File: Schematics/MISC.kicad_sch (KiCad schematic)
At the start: 7 parts, among them J6 I2C Header, J7 PWR, J8 I2S Header

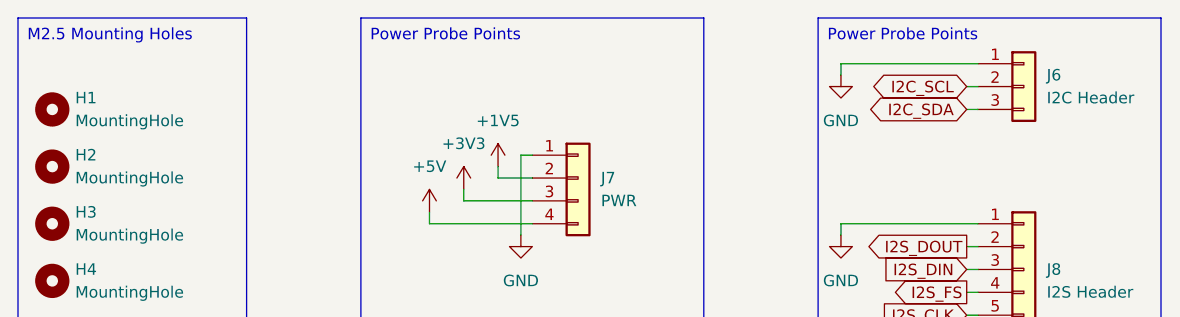
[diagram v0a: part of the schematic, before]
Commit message: Updated to KiCAD v9
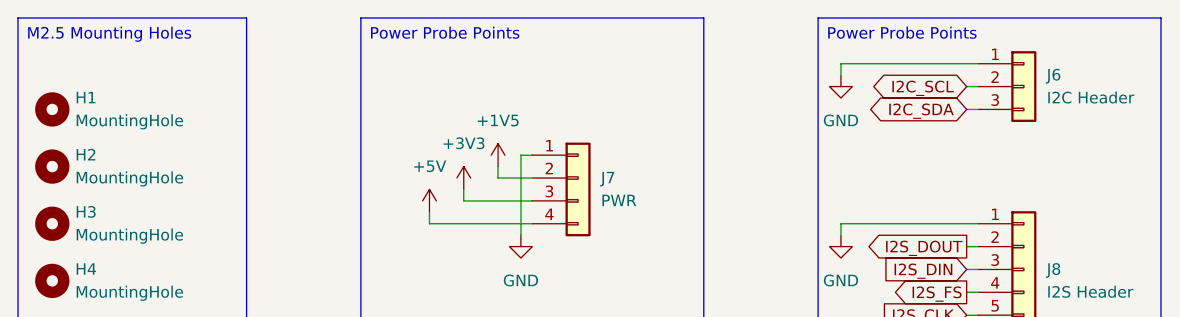
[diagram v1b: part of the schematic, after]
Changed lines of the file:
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@@
 (kicad_sch
-	(version 20231120)
+	(version 20250114)
 	(generator "eeschema")
-	(generator_version "8.0")
+	(generator_version "9.0")
 	(paper "A4")
-	(wire
-		(pts
-			(xy 116.84 31.75) (xy 116.84 30.48)
-		)
-		(stroke
-			(width 0)
-			(type default)
-		)
-	)
-	(wire
-		(pts
-			(xy 116.84 30.48) (xy 132.08 30.48)
-		)
-		(stroke
-			(width 0)
-			(type default)
-		)
-	)
-	(wire
-		(pts
-			(xy 74.93 45.72) (xy 74.93 44.45)
-		)
-		(stroke
-			(width 0)
-			(type default)
-		)
-	)
-	(wire
-		(pts
-			(xy 130.81 60.96) (xy 132.08 60.96)
-		)
-		(stroke
-			(width 0)
-			(type default)
-		)
-	)
-	(wire
-		(pts
-			(xy 130.81 58.42) (xy 132.08 58.42)
-		)
-		(stroke
-			(width 0)
-			(type default)
-		)
-	)
-	(wire
-		(pts
-			(xy 132.08 48.26) (xy 116.84 48.26)
-		)
-		(stroke
-			(width 0)
-			(type default)
-		)
-	)
-	(wire
-		(pts
-			(xy 130.81 35.56) (xy 132.08 35.56)
-		)
-		(stroke
-			(width 0)
-			(type default)
-		)
-	)
-	(wire
-		(pts
-			(xy 130.81 50.8) (xy 132.08 50.8)
-		)
-		(stroke
-			(width 0)
-			(type default)
-		)
-	)
-	(wire
-		(pts
-			(xy 130.81 33.02) (xy 132.08 33.02)
-		)
-		(stroke
-			(width 0)
-			(type default)
-		)
-	)
-	(wire
-		(pts
-			(xy 130.81 53.34) (xy 132.08 53.34)
-		)
-		(stroke
-			(width 0)
-			(type default)
-		)
-	)
-	(wire
-		(pts
-			(xy 81.28 40.64) (xy 81.28 49.53)
-		)
-		(stroke
-			(width 0)
-			(type default)
-		)
-	)
-	(wire
-		(pts
-			(xy 81.28 40.64) (xy 82.55 40.64)
-		)
-		(stroke
-			(width 0)
-			(type default)
-		)
-	)
-	(wire
-		(pts
-			(xy 71.12 46.99) (xy 71.12 48.26)
-		)
-		(stroke
-			(width 0)
-			(type default)
-		)
-	)
-	(wire
-		(pts
-			(xy 130.81 55.88) (xy 132.08 55.88)
-		)
-		(stroke
-			(width 0)
-			(type default)
-		)
-	)
-	(wire
-		(pts
-			(xy 116.84 48.26) (xy 116.84 49.53)
-		)
-		(stroke
-			(width 0)
-			(type default)
-		)
-	)
-	(wire
-		(pts
-			(xy 71.12 48.26) (xy 82.55 48.26)
-		)
-		(stroke
-			(width 0)
-			(type default)
-		)
-	)
-	(wire
-		(pts
-			(xy 82.55 45.72) (xy 74.93 45.72)
-		)
-		(stroke
-			(width 0)
-			(type default)
-		)
-	)
-	(wire
-		(pts
-			(xy 78.74 43.18) (xy 82.55 43.18)
-		)
-		(stroke
-			(width 0)
-			(type default)
-		)
-	)
-	(wire
-		(pts
-			(xy 78.74 41.91) (xy 78.74 43.18)
-		)
-		(stroke
-			(width 0)
-			(type default)
-		)
-	)
 	(text_box "M2.5 Mounting Holes"
 		(exclude_from_sim no)
 		(at 25.4 25.4 0)
 		(size 25.4 38.1)
+		(margins 0.9525 0.9525 0.9525 0.9525)
 		(stroke
 			(width 0)
@@
 		(at 114.3 25.4 0)
 		(size 38.1 38.1)
+		(margins 0.9525 0.9525 0.9525 0.9525)
 		(stroke
 			(width 0)
@@
 		(at 63.5 25.4 0)
 		(size 38.1 38.1)
+		(margins 0.9525 0.9525 0.9525 0.9525)
 		(stroke
 			(width 0)
@@
 		)
 	)
+	(wire
+		(pts
+			(xy 116.84 31.75) (xy 116.84 30.48)
+		)
+		(stroke
+			(width 0)
+			(type default)
+		)
+	)
+	(wire
+		(pts
+			(xy 116.84 30.48) (xy 132.08 30.48)
+		)
+		(stroke
+			(width 0)
+			(type default)
+		)
+	)
+	(wire
+		(pts
+			(xy 74.93 45.72) (xy 74.93 44.45)
+		)
+		(stroke
+			(width 0)
+			(type default)
+		)
+	)
+	(wire
+		(pts
+			(xy 130.81 60.96) (xy 132.08 60.96)
+		)
+		(stroke
+			(width 0)
+			(type default)
+		)
+	)
+	(wire
+		(pts
+			(xy 130.81 58.42) (xy 132.08 58.42)
+		)
+		(stroke
+			(width 0)
+			(type default)
+		)
+	)
+	(wire
+		(pts
+			(xy 132.08 48.26) (xy 116.84 48.26)
+		)
+		(stroke
+			(width 0)
+			(type default)
+		)
+	)
+	(wire
+		(pts
+			(xy 130.81 35.56) (xy 132.08 35.56)
+		)
+		(stroke
+			(width 0)
+			(type default)
+		)
+	)
+	(wire
+		(pts
+			(xy 130.81 50.8) (xy 132.08 50.8)
+		)
+		(stroke
+			(width 0)
+			(type default)
+		)
+	)
+	(wire
+		(pts
+			(xy 130.81 33.02) (xy 132.08 33.02)
+		)
+		(stroke
+			(width 0)
+			(type default)
+		)
+	)
+	(wire
+		(pts
+			(xy 130.81 53.34) (xy 132.08 53.34)
+		)
+		(stroke
+			(width 0)
+			(type default)
+		)
+	)
+	(wire
+		(pts
+			(xy 81.28 40.64) (xy 81.28 49.53)
+		)
+		(stroke
+			(width 0)
+			(type default)
+		)
+	)
+	(wire
+		(pts
+			(xy 81.28 40.64) (xy 82.55 40.64)
+		)
+		(stroke
+			(width 0)
+			(type default)
+		)
+	)
+	(wire
+		(pts
+			(xy 71.12 46.99) (xy 71.12 48.26)
+		)
+		(stroke
+			(width 0)
+			(type default)
+		)
+	)
+	(wire
+		(pts
+			(xy 130.81 55.88) (xy 132.08 55.88)
+		)
+		(stroke
+			(width 0)
+			(type default)
+		)
+	)
+	(wire
+		(pts
+			(xy 116.84 48.26) (xy 116.84 49.53)
+		)
+		(stroke
+			(width 0)
+			(type default)
+		)
+	)
+	(wire
+		(pts
+			(xy 71.12 48.26) (xy 82.55 48.26)
+		)
+		(stroke
+			(width 0)
+			(type default)
+		)
+	)
+	(wire
+		(pts
+			(xy 82.55 45.72) (xy 74.93 45.72)
+		)
+		(stroke
+			(width 0)
+			(type default)
+		)
+	)
+	(wire
+		(pts
+			(xy 78.74 43.18) (xy 82.55 43.18)
+		)
+		(stroke
+			(width 0)
+			(type default)
+		)
+	)
+	(wire
+		(pts
+			(xy 78.74 41.91) (xy 78.74 43.18)
+		)
+		(stroke
+			(width 0)
+			(type default)
+		)
+	)

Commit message: File labelling
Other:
- note added: "Drawn by Harvey McBurney, Nicolas Viale"
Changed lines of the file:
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@@
 	(generator_version "9.0")
 	(paper "A4")
+	(text "Drawn by Harvey McBurney, Nicolas Viale"
+		(exclude_from_sim no)
+		(at 210.82 169.926 0)
+		(effects
+			(font
+				(size 2 2)
+				(thickness 0.6)
+				(bold yes)
+			)
+		)
+	)
 	(text_box "M2.5 Mounting Holes"
 		(exclude_from_sim no)

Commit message: Tidied up Schematic
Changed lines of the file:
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@@
 		)
 	)
-	(text_box "Power Probe Points"
+	(text_box "Serial Probe Points"
 		(exclude_from_sim no)
 		(at 114.3 25.4 0)
@@
 		(stroke
 			(width 0)
-			(type default)
+			(type solid)
 		)
 		(fill
